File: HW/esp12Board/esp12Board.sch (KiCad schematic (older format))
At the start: 49 parts, among them IC1 TPS54331DR, J1 Conn_01x07, J2 Conn_01x03, J3 Conn_02x05_Odd_Even, J4 Conn_01x02, J5 Conn_01x03, J6 Conn_01x03, Q1 S8050, Q2 S8050, SW1 SW_Push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

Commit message: fixes
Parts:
- IC1: symbol SamacSys_Parts:TPS54331DR -> esp12Board-rescue:TPS54331DR-SamacSys_Parts
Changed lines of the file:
@@
 $EndComp
 $Comp
-L SamacSys_Parts:TPS54331DR IC1
+L esp12Board-rescue:TPS54331DR-SamacSys_Parts IC1
 U 1 1 5FE6A6A2
 P 6700 2450

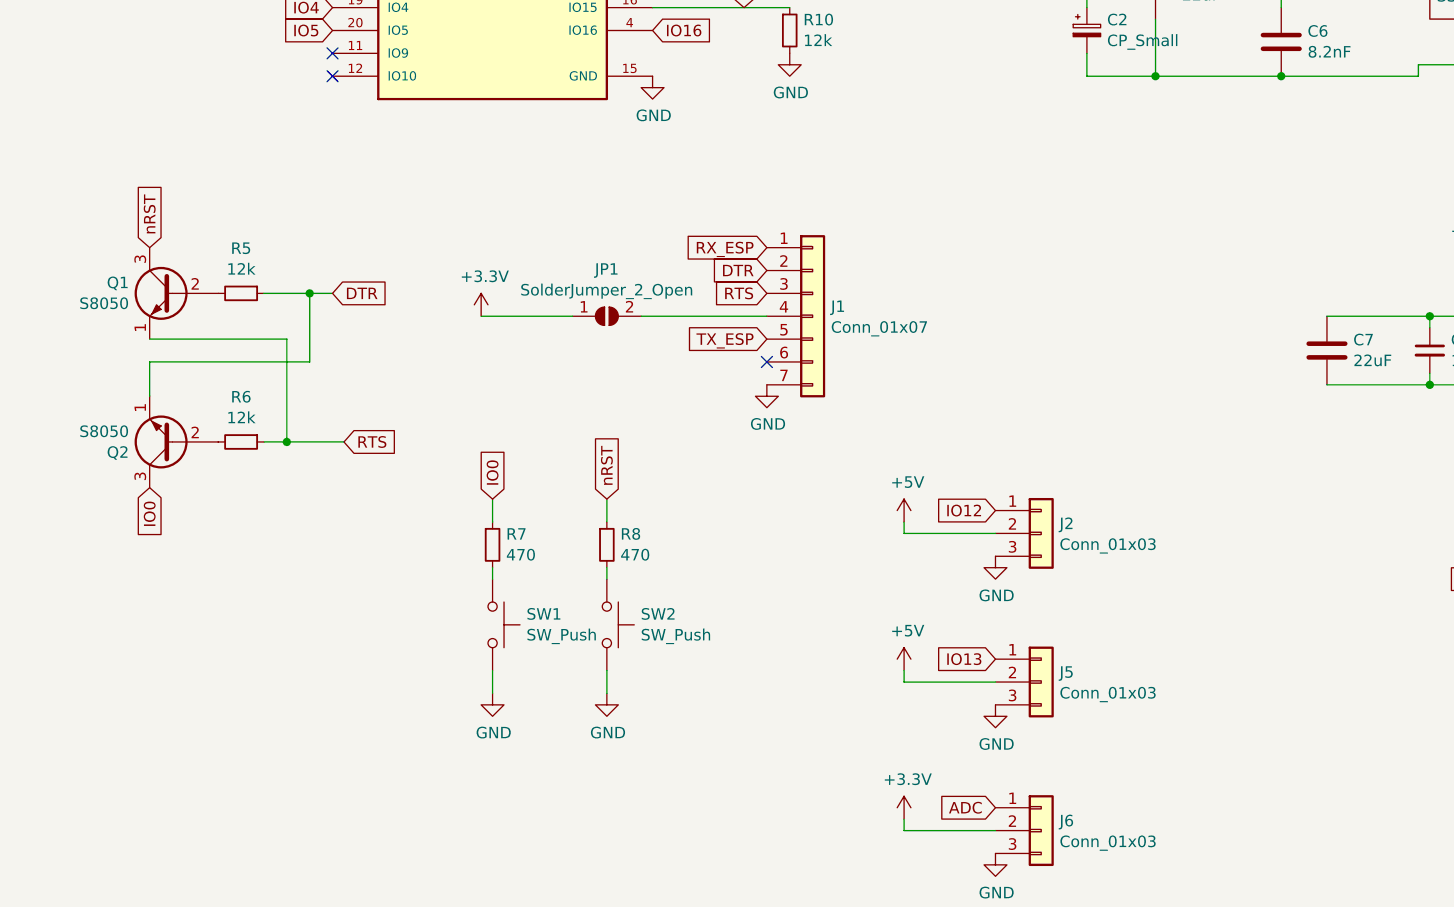
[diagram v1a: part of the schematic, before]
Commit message: Fixed npn orientation added contacts, remove boot sw
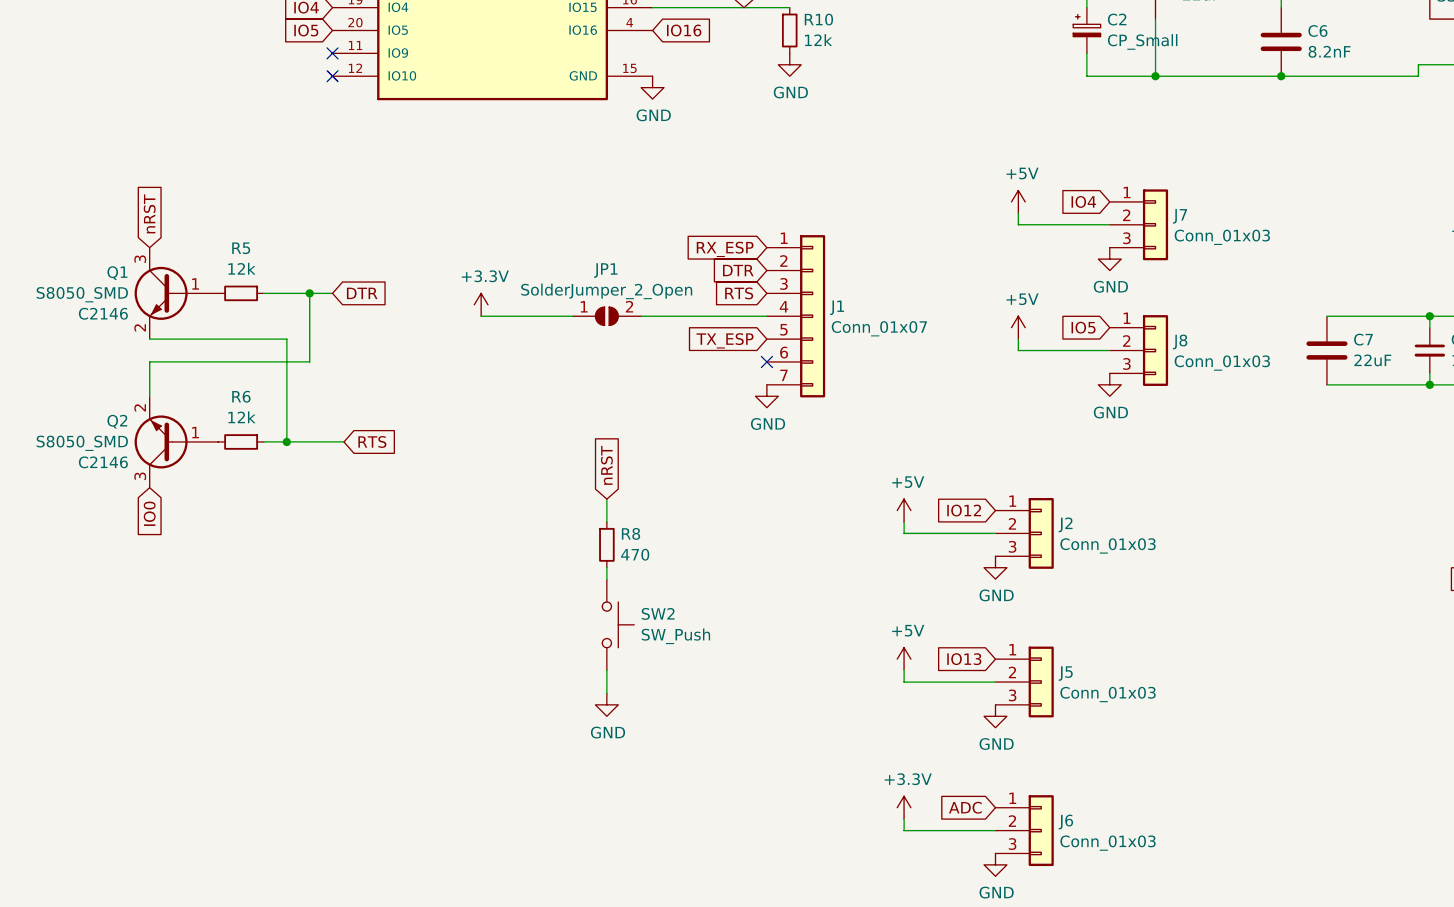
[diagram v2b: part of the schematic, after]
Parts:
- removed Q1, Q2: S8050, Package_TO_SOT_SMD:SOT-23, symbol Transistor_BJT:S8050
- removed R7: 470, Resistor_SMD:R_0805_2012Metric_Pad1.15x1.40mm_HandSolder, symbol Device:R_Small
- removed SW1: SW_Push, Button_Switch_THT:SW_PUSH_6mm, symbol Switch:SW_Push
- added J7, J8: Conn_01x03, Connector_PinHeader_2.54mm:PinHeader_1x03_P2.54mm_Vertical, symbol Connector_Generic:Conn_01x03
- added Q1, Q2: S8050_SMD, Package_TO_SOT_SMD:SOT-23, symbol tobias_Library:S8050_SMD
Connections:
- net +5V: now also J7.2 (Pin_2), J8.2 (Pin_2)
- net DTR: now also Q2.2 (E)
- net GND: now also J7.3 (Pin_3), J8.3 (Pin_3)
- net IO0: now also Q2.3 (C)
- net IO4: now also J7.1 (Pin_1)
- net IO5: now also J8.1 (Pin_1)
- net RTS: now also Q1.2 (E)
- net nRST: now also Q1.3 (C)
- net at R5.2: now also Q1.1 (B)
- net at R6.2: now also Q2.1 (B)
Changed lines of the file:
@@
 	1950 1800 1650 1800
-$Comp
-L Transistor_BJT:S8050 Q1
-U 1 1 5FEC3B79
-P 1400 4050
-F 0 "Q1" H 1590 4096 50  0000 L CNN
-F 1 "S8050" H 1590 4005 50  0000 L CNN
-F 2 "Package_TO_SOT_SMD:SOT-23" H 1600 3975 50  0001 L CIN
-F 3 "http://www.unisonic.com.tw/datasheet/S8050.pdf" H 1400 4050 50  0001 L CNN
-F 4 "C2146" H 1400 4050 50  0001 C CNN "LCSC"
-	1    1400 4050
-	-1   0    0    -1
-$EndComp
-$Comp
-L Transistor_BJT:S8050 Q2
-U 1 1 5FEC4B5D
-P 1400 4700
-F 0 "Q2" H 1590 4746 50  0000 L CNN
-F 1 "S8050" H 1590 4655 50  0000 L CNN
-F 2 "Package_TO_SOT_SMD:SOT-23" H 1600 4625 50  0001 L CIN
-F 3 "http://www.unisonic.com.tw/datasheet/S8050.pdf" H 1400 4700 50  0001 L CNN
-F 4 "C2146" H 1400 4700 50  0001 C CNN "LCSC"
-	1    1400 4700
-	-1   0    0    1
-$EndComp
 $Comp
 L Device:R_Small R5
@@
 Text GLabel 3300 4950 1    50   Input ~ 0
 nRST
-Text GLabel 2800 4950 1    50   Input ~ 0
-IO0
-$Comp
-L Device:R_Small R7
-U 1 1 5FF09F68
-P 2800 5150
-F 0 "R7" H 2859 5196 50  0000 L CNN
-F 1 "470" H 2859 5105 50  0000 L CNN
-F 2 "Resistor_SMD:R_0805_2012Metric_Pad1.15x1.40mm_HandSolder" H 2800 5150 50  0001 C CNN
-F 3 "~" H 2800 5150 50  0001 C CNN
-F 4 "C17710" H 2800 5150 50  0001 C CNN "LCSC"
-	1    2800 5150
-	1    0    0    -1
-$EndComp
-$Comp
-L Switch:SW_Push SW1
-U 1 1 5FF0A11F
-P 2800 5500
-F 0 "SW1" V 2754 5648 50  0000 L CNN
-F 1 "SW_Push" V 2845 5648 50  0000 L CNN
-F 2 "Button_Switch_THT:SW_PUSH_6mm" H 2800 5700 50  0001 C CNN
-F 3 "~" H 2800 5700 50  0001 C CNN
-	1    2800 5500
-	0    1    1    0
-$EndComp
 $Comp
 L power:GND #PWR0118
@@
 	1    0    0    -1
 $EndComp
-$Comp
-L power:GND #PWR0119
-U 1 1 5FF0A72E
-P 2800 5800
-F 0 "#PWR0119" H 2800 5550 50  0001 C CNN
-F 1 "GND" H 2805 5627 50  0000 C CNN
-F 2 "" H 2800 5800 50  0001 C CNN
-F 3 "" H 2800 5800 50  0001 C CNN
-	1    2800 5800
-	1    0    0    -1
-$EndComp
-Wire Wire Line
-	2800 5800 2800 5700
-Wire Wire Line
-	2800 5050 2800 4950
-Wire Wire Line
-	2800 5300 2800 5250
 Wire Wire Line
 	3300 5800 3300 5700
@@
 	1    0    0    -1
 $EndComp
+$Comp
+L tobias_Library:S8050_SMD Q1
+U 1 1 60A77888
+P 1400 4050
+F 0 "Q1" H 1591 4141 50  0000 L CNN
+F 1 "S8050_SMD" H 1591 4050 50  0000 L CNN
+F 2 "Package_TO_SOT_SMD:SOT-23" H 1600 3975 50  0001 L CIN
+F 3 "http://www.unisonic.com.tw/datasheet/S8050.pdf" H 1400 4050 50  0001 L CNN
+F 4 "C2146" H 1591 3959 50  0000 L CNN "LCSC"
+	1    1400 4050
+	-1   0    0    -1
+$EndComp
+$Comp
+L tobias_Library:S8050_SMD Q2
+U 1 1 60A79235
+P 1400 4700
+F 0 "Q2" H 1591 4609 50  0000 L CNN
+F 1 "S8050_SMD" H 1591 4700 50  0000 L CNN
+F 2 "Package_TO_SOT_SMD:SOT-23" H 1600 4625 50  0001 L CIN
+F 3 "http://www.unisonic.com.tw/datasheet/S8050.pdf" H 1400 4700 50  0001 L CNN
+F 4 "C2146" H 1591 4791 50  0000 L CNN "LCSC"
+	1    1400 4700
+	-1   0    0    1
+$EndComp
+$Comp
+L Connector_Generic:Conn_01x03 J7
+U 1 1 60A83B49
+P 5700 3750
+F 0 "J7" H 5780 3792 50  0000 L CNN
+F 1 "Conn_01x03" H 5780 3701 50  0000 L CNN
+F 2 "Connector_PinHeader_2.54mm:PinHeader_1x03_P2.54mm_Vertical" H 5700 3750 50  0001 C CNN
+F 3 "~" H 5700 3750 50  0001 C CNN
+	1    5700 3750
+	1    0    0    -1
+$EndComp
+$Comp
+L power:+5V #PWR0110
+U 1 1 60A83B4F
+P 5100 3700
+F 0 "#PWR0110" H 5100 3550 50  0001 C CNN
+F 1 "+5V" H 5115 3873 50  0000 C CNN
+F 2 "" H 5100 3700 50  0001 C CNN
+F 3 "" H 5100 3700 50  0001 C CNN
+	1    5100 3700
+	1    0    0    -1
+$EndComp
+Wire Wire Line
+	5500 3750 5100 3750
+Wire Wire Line
+	5100 3750 5100 3700
+$Comp
+L power:GND #PWR0119
+U 1 1 60A83B57
+P 5500 3850
+F 0 "#PWR0119" H 5500 3600 50  0001 C CNN
+F 1 "GND" H 5505 3677 50  0000 C CNN
+F 2 "" H 5500 3850 50  0001 C CNN
+F 3 "" H 5500 3850 50  0001 C CNN
+	1    5500 3850
+	1    0    0    -1
+$EndComp
+Text GLabel 5500 3650 0    50   Input ~ 0
+IO4
+$Comp
+L Connector_Generic:Conn_01x03 J8
+U 1 1 60A888B2
+P 5700 4300
+F 0 "J8" H 5780 4342 50  0000 L CNN
+F 1 "Conn_01x03" H 5780 4251 50  0000 L CNN
+F 2 "Connector_PinHeader_2.54mm:PinHeader_1x03_P2.54mm_Vertical" H 5700 4300 50  0001 C CNN
+F 3 "~" H 5700 4300 50  0001 C CNN
+	1    5700 4300
+	1    0    0    -1
+$EndComp
+$Comp
+L power:+5V #PWR0131
+U 1 1 60A888B8
+P 5100 4250
+F 0 "#PWR0131" H 5100 4100 50  0001 C CNN
+F 1 "+5V" H 5115 4423 50  0000 C CNN
+F 2 "" H 5100 4250 50  0001 C CNN
+F 3 "" H 5100 4250 50  0001 C CNN
+	1    5100 4250
+	1    0    0    -1
+$EndComp
+Wire Wire Line
+	5500 4300 5100 4300
+Wire Wire Line
+	5100 4300 5100 4250
+$Comp
+L power:GND #PWR0132
+U 1 1 60A888C0
+P 5500 4400
+F 0 "#PWR0132" H 5500 4150 50  0001 C CNN
+F 1 "GND" H 5505 4227 50  0000 C CNN
+F 2 "" H 5500 4400 50  0001 C CNN
+F 3 "" H 5500 4400 50  0001 C CNN
+	1    5500 4400
+	1    0    0    -1
+$EndComp
+Text GLabel 5500 4200 0    50   Input ~ 0
+IO5
 $EndSCHEMATC
